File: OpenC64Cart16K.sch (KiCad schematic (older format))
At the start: 11 parts, among them J1 OSHW_LOGO, J2 PEG_HOLE, P1 CONN_01X03, P2 CONN_01X03, SW1 RESET_SW, U1 C64-Exp-Port, U2 27512

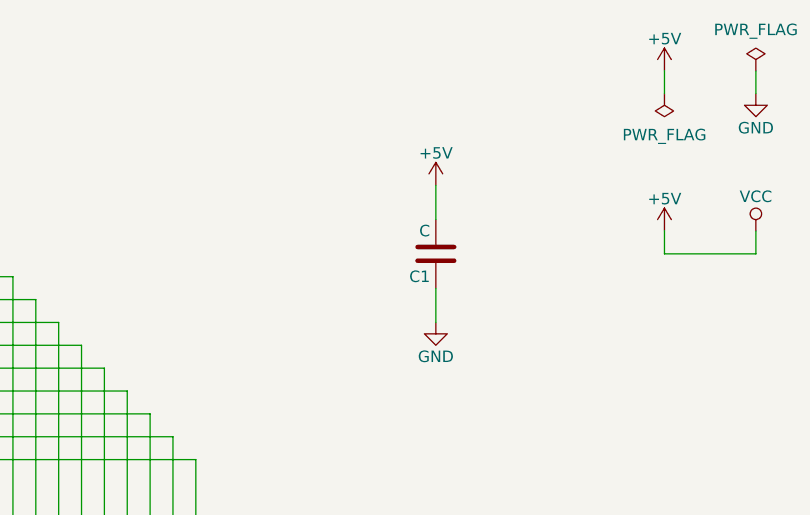
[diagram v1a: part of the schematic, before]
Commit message: Fix cap value
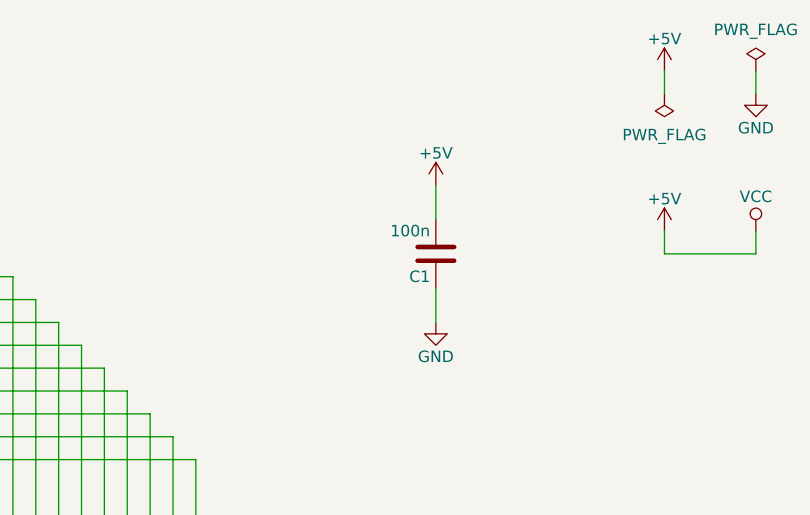
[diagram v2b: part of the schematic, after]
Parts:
- C1: value C -> 100n
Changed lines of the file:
@@
 P 9100 1550
 F 0 "C1" H 9125 1650 50  0000 L CNN
-F 1 "C" H 9125 1450 50  0000 L CNN
+F 1 "100n" H 9125 1450 50  0000 L CNN
 F 2 "OpenC64Cart16K:C_0805+THT" H 9138 1400 50  0001 C CNN
 F 3 "" H 9100 1550 50  0000 C CNN

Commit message: Use THT/SMD combo pads for all components
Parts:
- D1, D2: footprint Diodes_THT:D_DO-35_SOD27_P7.62mm_Horizontal -> OpenC64Cart16K:D_DO35+SMA
- J1: footprint w_logo:Logo_copper_OSHW_12x13mm -> w_logo:Logo_copper_OSHW_6x6mm
- R1: footprint Resistors_THT:R_Axial_DIN0204_L3.6mm_D1.6mm_P7.62mm_Horizontal -> OpenC64Cart16K:R_0805+THT-7.62mm
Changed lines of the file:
@@
 F 0 "J1" H 10750 6350 50  0000 C CNN
 F 1 "OSHW_LOGO" H 10750 6150 50  0000 C CNN
-F 2 "w_logo:Logo_copper_OSHW_12x13mm" H 10750 6250 50  0001 C CNN
+F 2 "w_logo:Logo_copper_OSHW_6x6mm" H 10750 6250 50  0001 C CNN
 F 3 "" H 10750 6250 50  0001 C CNN
 	1    10750 6250
@@
 F 0 "D1" H 7225 6050 50  0000 C CNN
 F 1 "1N4148" H 7225 5850 50  0000 C CNN
-F 2 "Diodes_THT:D_DO-35_SOD27_P7.62mm_Horizontal" H 7225 5950 50  0001 C CNN
+F 2 "OpenC64Cart16K:D_DO35+SMA" H 7225 5950 50  0001 C CNN
 F 3 "" H 7225 5950 50  0001 C CNN
 	1    7225 5950
@@
 F 0 "D2" H 7600 6225 50  0000 C CNN
 F 1 "1N4148" H 7600 6025 50  0000 C CNN
-F 2 "Diodes_THT:D_DO-35_SOD27_P7.62mm_Horizontal" H 7600 6125 50  0001 C CNN
+F 2 "OpenC64Cart16K:D_DO35+SMA" H 7600 6125 50  0001 C CNN
 F 3 "" H 7600 6125 50  0001 C CNN
 	1    7600 6125
@@
 F 0 "R1" V 8480 5950 50  0000 C CNN
 F 1 "10k" V 8400 5950 50  0000 C CNN
-F 2 "Resistors_THT:R_Axial_DIN0204_L3.6mm_D1.6mm_P7.62mm_Horizontal" V 8330 5950 50  0001 C CNN
+F 2 "OpenC64Cart16K:R_0805+THT-7.62mm" V 8330 5950 50  0001 C CNN
 F 3 "" H 8400 5950 50  0001 C CNN
 	1    8400 5950
